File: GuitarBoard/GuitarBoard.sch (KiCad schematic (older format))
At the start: 50 parts, among them IC1 CD4069UBE, J1 Pickups, J2 Input Jack, J3 Bridge Ground, J8 Output Jack, J9 Amp, Q1 2N3904, Q2 2N3904, SW1 Amp Knob Switch, SW2 Volume DPDT A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

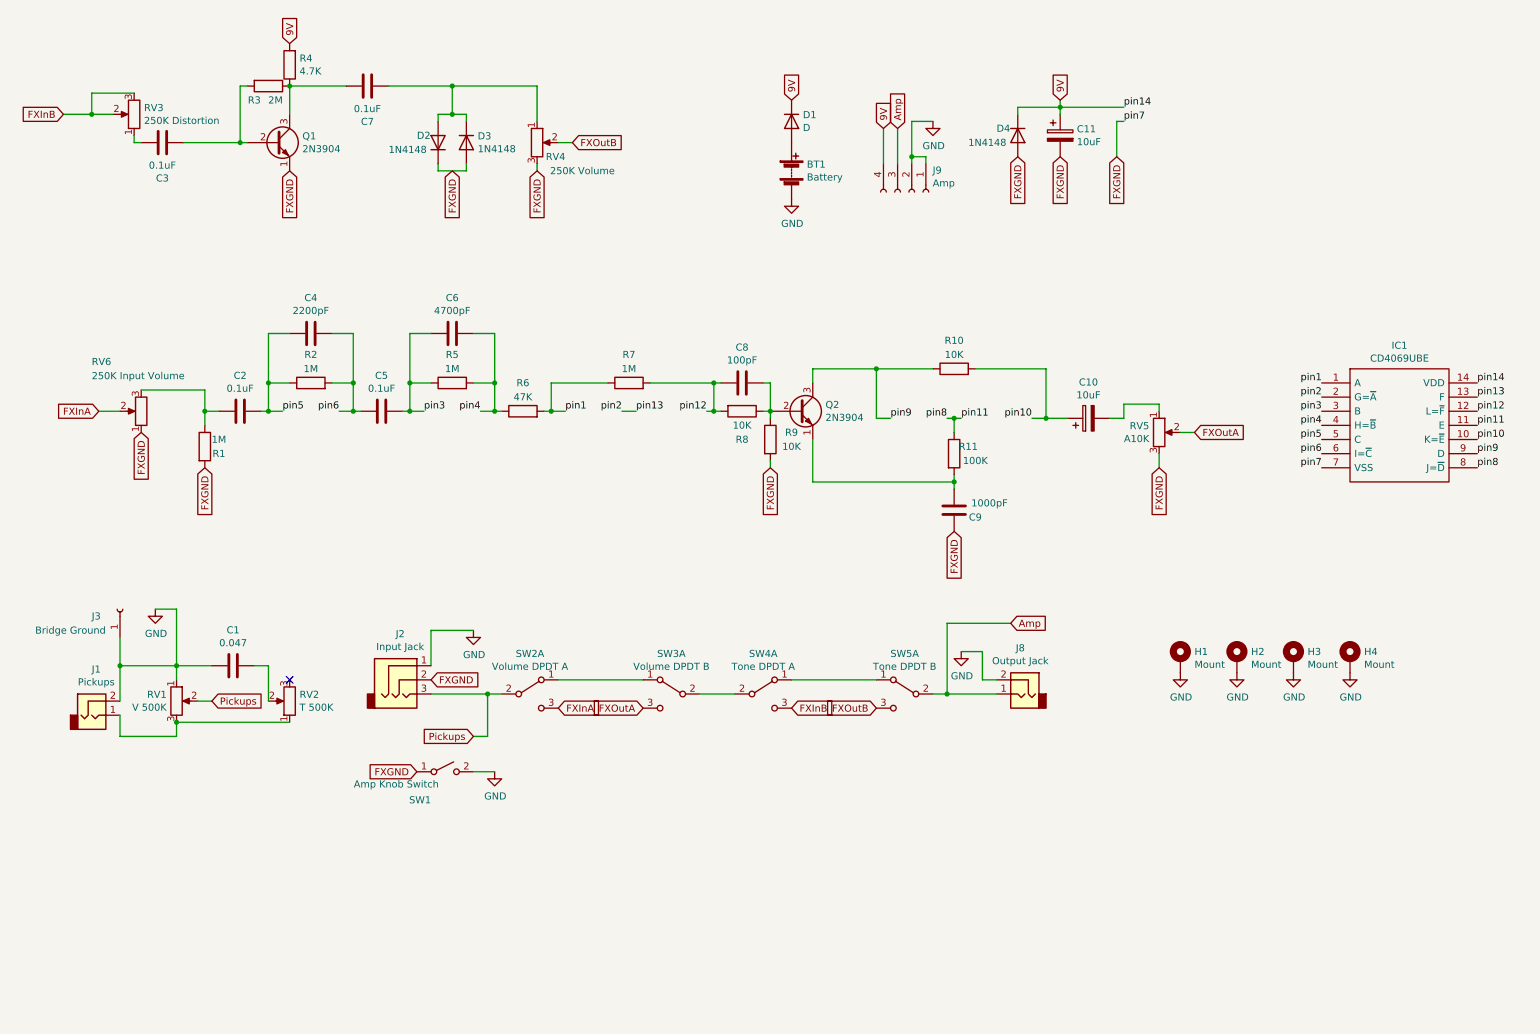
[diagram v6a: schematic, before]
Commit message: Made minor improvements. Might need to make a couple more before updating pcb
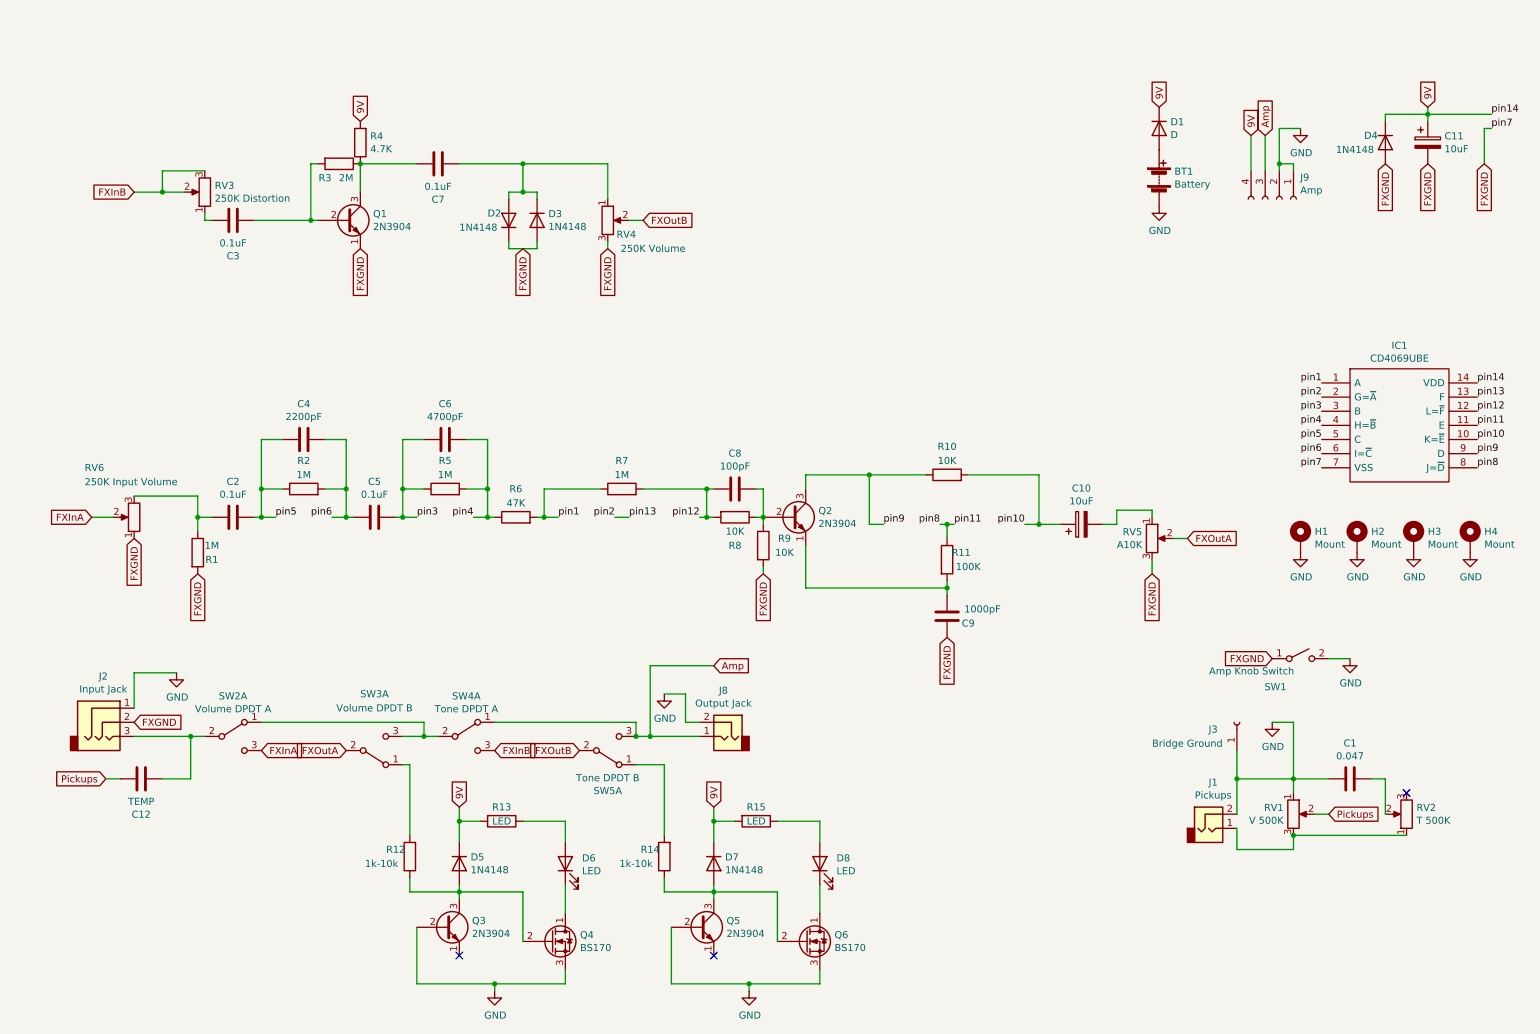
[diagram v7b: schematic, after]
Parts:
- added C12: TEMP, libraries:C_Flat_L7.2_H6.5, symbol Device:C
- added D5, D7: 1N4148, Diode_THT:D_DO-35_SOD27_P7.62mm_Horizontal, symbol Diode:1N4148
- added D6, D8: LED, LED_THT:LED_D5.0mm, symbol Device:LED
- added Q3, Q5: 2N3904, Package_TO_SOT_THT:TO-92_Inline, symbol Transistor_BJT:2N3904
- added Q4, Q6: BS170, Package_TO_SOT_THT:TO-92_Inline, symbol Transistor_FET:BS170
- added R12, R14: 1k-10k, Resistor_THT:R_Axial_DIN0207_L6.3mm_D2.5mm_P10.16mm_Horizontal, symbol Device:R
- added R13, R15: LED, Resistor_THT:R_Axial_DIN0207_L6.3mm_D2.5mm_P10.16mm_Horizontal, symbol Device:R
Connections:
- net 9V: now also D5.1 (K), D7.1 (K), R13.2, R15.2
- net Amp: now also SW4.1 (A), SW5.3 (C); no longer SW5.2 (B)
- net FXOutA: now also SW3.2 (B); no longer SW3.3 (C)
- net FXOutB: now also SW5.2 (B); no longer SW5.3 (C)
- net GND: now also Q3.2 (B), Q4.3 (S), Q5.2 (B), Q6.3 (S)
- net Pickups: now also C12.1; no longer J2.3, SW2.2 (B)
- net at SW2.1 (A): now also SW3.3 (C), SW4.2 (B); no longer SW3.1 (A)
- net at SW5.1 (A): now also R14.2; no longer SW4.1 (A)
- new net: C12.2, J2.3, SW2.2 (B)
- new net: R12.2, SW3.1 (A)
- new net: D5.2 (A), Q3.3 (C), Q4.2 (G), R12.1
- new net: D6.2 (A), R13.1
- new net: D6.1 (K), Q4.1 (D)
- new net: D7.2 (A), Q5.3 (C), Q6.2 (G), R14.1
- new net: D8.2 (A), R15.1
- new net: D8.1 (K), Q6.1 (D)
- no-connect marks 1 -> 3
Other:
- moved on the sheet: BT1, C1, C10, C11, C2, C3, C4, C5, C6, C7, C8, C9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

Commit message: Built shake tremolo inside guitar board. Added separate schematic sheets since I ran out of space
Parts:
- removed C10, C11: 10uF, Capacitor_THT:CP_Axial_L10.0mm_D6.0mm_P15.00mm_Horizontal, symbol Device:CP
- removed C2, C5: 0.1uF, libraries:C_Flat_L7.2_H6.5, symbol Device:C
- removed C4: 2200pF, libraries:C_Flat_L7.2_H6.5, symbol Device:C
- removed C6: 4700pF, libraries:C_Flat_L7.2_H6.5, symbol Device:C
- removed C8: 100pF, libraries:C_Flat_L7.2_H6.5, symbol Device:C
- removed C9: 1000pF, libraries:C_Flat_L7.2_H6.5, symbol Device:C
- removed D4: 1N4148, Diode_THT:D_DO-35_SOD27_P7.62mm_Horizontal, symbol Diode:1N4148
- removed IC1: CD4069UBE, SamacSys_Parts:DIP794W53P254L1930H508Q14N, symbol SamacSys_Parts:CD4069UBE
- removed Q2: 2N3904, Package_TO_SOT_THT:TO-92_Inline, symbol Transistor_BJT:2N3904
- removed R1, R2, R5, R7: 1M, Resistor_THT:R_Axial_DIN0207_L6.3mm_D2.5mm_P10.16mm_Horizontal, symbol Device:R
- removed R10, R8, R9: 10K, Resistor_THT:R_Axial_DIN0207_L6.3mm_D2.5mm_P10.16mm_Horizontal, symbol Device:R
- removed R11: 100K, Resistor_THT:R_Axial_DIN0207_L6.3mm_D2.5mm_P10.16mm_Horizontal, symbol Device:R
- removed R6: 47K, Resistor_THT:R_Axial_DIN0207_L6.3mm_D2.5mm_P10.16mm_Horizontal, symbol Device:R
- removed RV5: A10K, Potentiometer_THT:Potentiometer_Bourns_3386F_Vertical, symbol Device:R_POT
- removed RV6: 250K Input Volume, Potentiometer_THT:Potentiometer_Bourns_3386F_Vertical, symbol Device:R_POT
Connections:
- net FXInA: now also RV3.2, RV3.3
- net FXInB: no longer RV3.2, RV3.3
- net FXOutA: now also RV4.2
- net FXOutB: no longer RV4.2
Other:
- moved on the sheet: C3, C7, D2, D3, Q1, R3, R4, RV3, RV4
